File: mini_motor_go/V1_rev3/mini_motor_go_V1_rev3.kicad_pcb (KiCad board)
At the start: 4 copper layers, 72 x 47 mm, 97 parts, among them J1 CONN_03POLAR_LOCK, J10 Conn_01x02_Pin, J11 USB4520-03-0-A_REVA, J12 BM05B-SRSS-TB_LF__SN_, J13 BM05B-SRSS-TB_LF__SN_, J2 CONN_03POLAR_LOCK, J3 I2C_STANDARDQWIIC, J5 I2C_STANDARDQWIIC, J9 Conn_01x09_Pin, U1 ESP32-S3-WROOM-1, U2 TMC6300, U3 INA2181, U4 INA2181, U5 TMC6300, U6 AZ1117C, U7 TPS562208

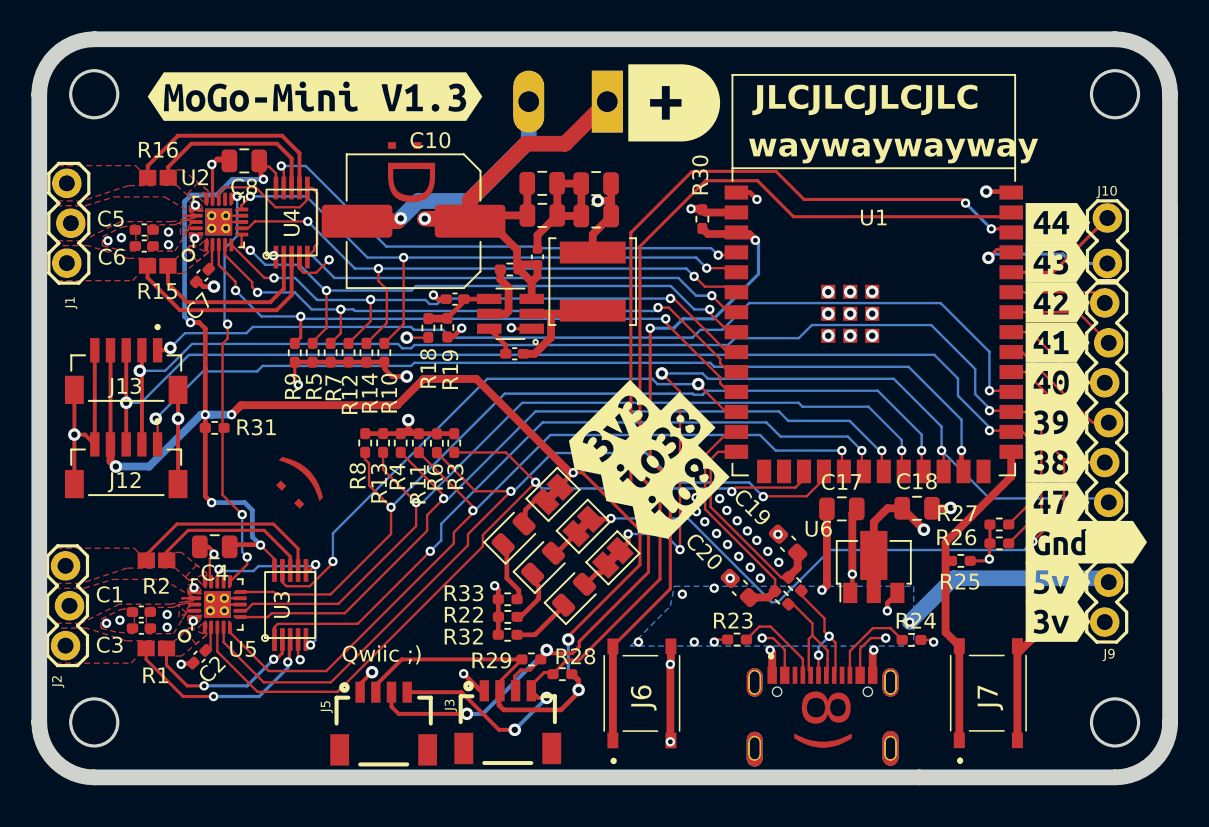
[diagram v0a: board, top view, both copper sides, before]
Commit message: changed .1uf caps to 0805 C14-C16
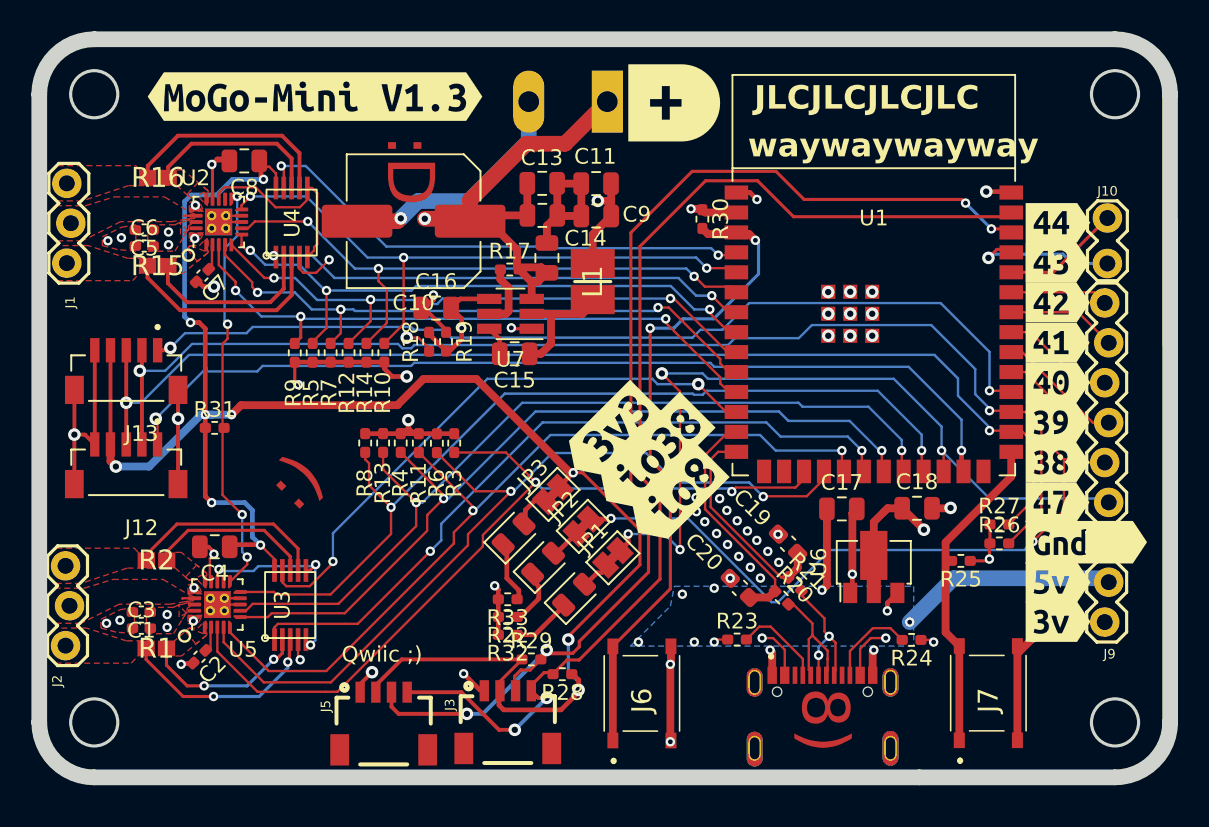
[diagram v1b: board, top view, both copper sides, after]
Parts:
- C1, C2, C3, C5, C6, C7: footprint mg_mini_v1r3:C_0402_1005Metric_Pad0.74x0.62mm_HandSolder -> Capacitor_SMD:C_0402_1005Metric_Pad0.74x0.62mm_HandSolder
- C10: footprint mg_mini_v1r3:C_Elec_8x10.2 -> Capacitor_SMD:C_Elec_8x10.2
- C11, C12, C13, C17, C18, C9: footprint mg_mini_v1r3:C_0805_2012Metric -> Capacitor_SMD:C_0805_2012Metric
- C14: footprint mg_mini_v1r3:C_0402_1005Metric -> Capacitor_SMD:C_0805_2012Metric
- C15, C16: footprint mg_mini_v1r3:C_0402_1005Metric_Pad0.74x0.62mm_HandSolder -> Capacitor_SMD:C_0805_2012Metric
- J12, J13: footprint mg_mini_v1r3:JST_BM05B-SRSS-TB_LF__SN_ -> SnapEDA Library:JST_BM05B-SRSS-TB_LF__SN_
- J6, J7: footprint mg_mini_v1r3:PTS526SM08SMTR2LFS -> aaa_SamacSys_Parts:PTS526SM08SMTR2LFS
- JP1, JP2, JP3: footprint mg_mini_v1r3:SolderJumper-2_P1.3mm_Bridged_Pad1.0x1.5mm -> Jumper:SolderJumper-2_P1.3mm_Bridged_Pad1.0x1.5mm
- L1: footprint mg_mini_v1r3:L_Changjiang_FNR5020S -> aaa_SamacSys_Parts:INDC3225X120N
- R1, R15, R16, R2: footprint mg_mini_v1r3:RESC1608X55N -> aaa_SamacSys_Parts:RESC1608X55N
- R10, R11, R12, R13, R14, R17, R18, R19, R20, R21, R22, R23, R24, R25, R26, R27, R28, R29, R3, R30, R31, R32, R33, R4, R5, R6, R7, R8, R9: footprint mg_mini_v1r3:R_0402_1005Metric_Pad0.72x0.64mm_HandSolder -> Resistor_SMD:R_0402_1005Metric_Pad0.72x0.64mm_HandSolder
- U6: footprint mg_mini_v1r3:SOT-89-3 -> Package_TO_SOT_SMD:SOT-89-3
- U7: footprint mg_mini_v1r3:SOT-23-6_Handsoldering -> Package_TO_SOT_SMD:SOT-23-6_Handsoldering
- moved C16 1.33 mm to (139.8, 66.6)
- moved R19 0.90 mm to (140.4, 68.8), turned to -90 degrees
- moved R18 0.88 mm to (139.3, 68.8)
- moved C14 0.60 mm to (146.8, 63.4)
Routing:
- net Net-(U7-VFB): track 4.38 -> 7.97 mm, vias 0 -> 1
- net +5V: track 35.0 -> 36.3 mm, vias 12 -> 11
- net Net-(C11-Pad2): track 9.87 -> 9.23 mm
- net +BATT: track 33.7 -> 34.3 mm

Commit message: revision meeting with tom edits
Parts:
- J8: moved to F.Cu
- L1: footprint aaa_SamacSys_Parts:INDC3225X120N -> Inductor_SMD:L_Changjiang_FNR5020S
- R1, R15, R16, R2: footprint aaa_SamacSys_Parts:RESC1608X55N -> Resistor_SMD:R_0805_2012Metric
- moved L1 0.58 mm to (150.2, 64.6)
- moved C14 0.36 mm to (146.5, 63.4)
- moved R17 0.29 mm to (144.2, 64.2)
- moved R15 0.28 mm to (122.1, 64.2)
- moved R1 0.23 mm to (121.9, 88.5)
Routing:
- net +BATT: track 34.3 -> 33.4 mm

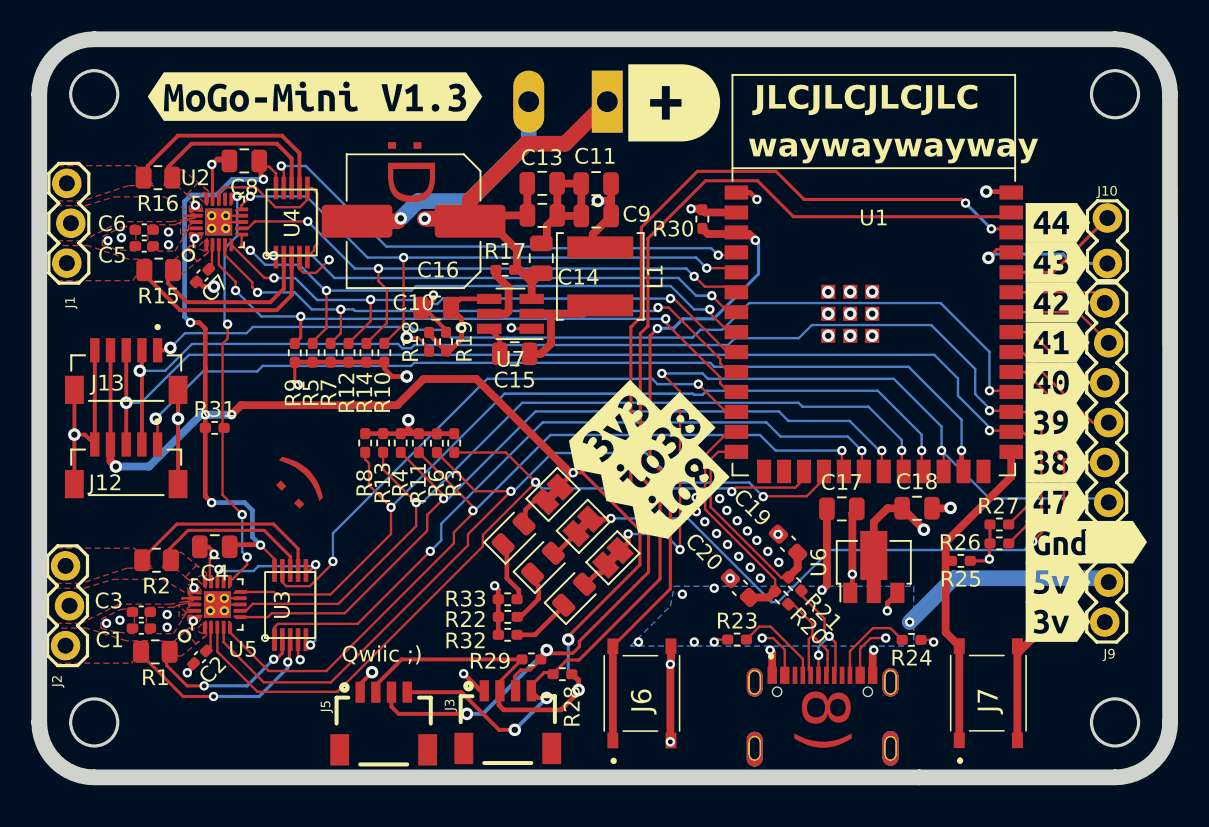
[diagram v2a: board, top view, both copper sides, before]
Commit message: fix indicator led silkscreen io8 to io47
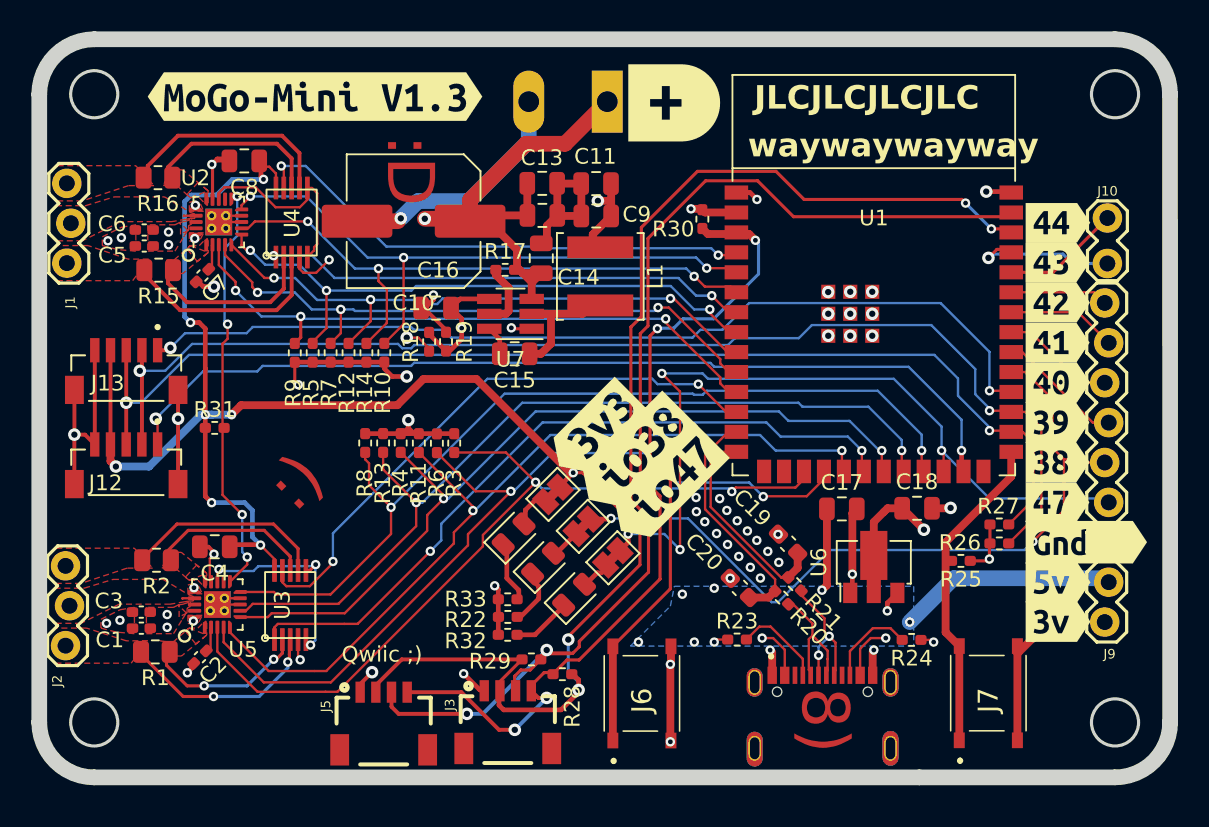
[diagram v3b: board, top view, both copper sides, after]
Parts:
- removed kibuzzard-65733972: G***, kibuzzard-65733972
- added kibuzzard-66038D2F: G***, kibuzzard-66038D2F, F.Cu at (154.4, 77.9)
- moved kibuzzard-65733965 1.11 mm to (152.4, 75.9)
- moved kibuzzard-6573395A 1.00 mm to (149.9, 74.4)
